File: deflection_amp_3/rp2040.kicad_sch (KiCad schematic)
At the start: 44 parts, among them SW1 RESET, SW2 PROG, U5 W25Q128JVS, U6 RP2040, U7 MCP4822, U8 MCP4822, Y1 ABM8-272-T3

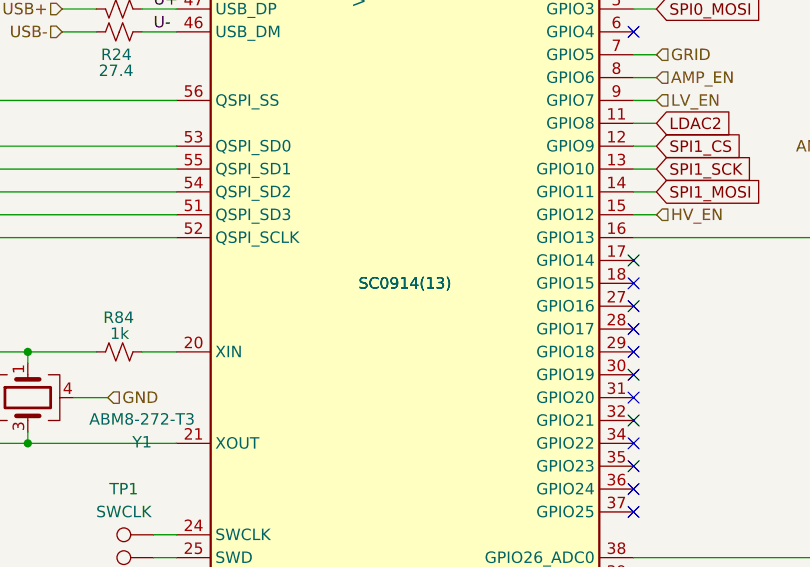
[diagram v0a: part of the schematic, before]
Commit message: fixed BOM + DAC footprint
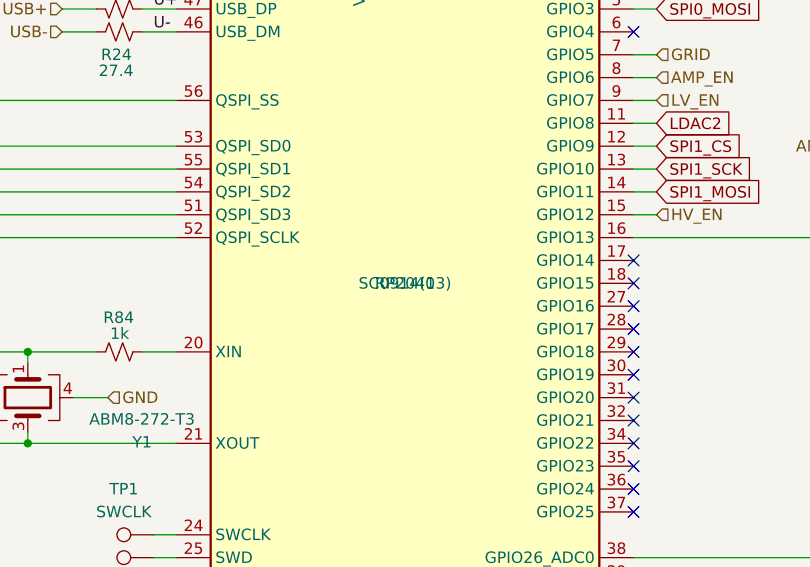
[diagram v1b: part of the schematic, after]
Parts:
- U6: JLCPCB P/N SC0914(13) -> RP2040
- U7, U8: footprint Package_SO:SOIC-8_5.3x5.3mm_P1.27mm -> MCP4822-E_SN:SOIC127P599X175-8N; JLCPCB P/N double check footprint -> MCP4822-E/SN
- Y1: JLCPCB P/N (none) -> ABM8-272-T3
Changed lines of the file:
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@@
 			)
 		)
-		(property "JLCPCB P/N" ""
+		(property "JLCPCB P/N" "ABM8-272-T3"
 			(at 96.52 114.3 0)
 			(effects
@@
 			)
 		)
-		(property "JLCPCB P/N" "SC0914(13)"
+		(property "JLCPCB P/N" "RP2040"
 			(at 138.43 101.6 0)
 			(effects
@@
 			)
 		)
-		(property "Footprint" "Package_SO:SOIC-8_5.3x5.3mm_P1.27mm"
+		(property "Footprint" "MCP4822-E_SN:SOIC127P599X175-8N"
 			(at 262.89 96.52 0)
 			(effects
@@
 			)
 		)
-		(property "JLCPCB P/N" "double check footprint"
+		(property "JLCPCB P/N" "MCP4822-E/SN"
 			(at 242.57 88.9 0)
 			(effects
@@
 			)
 		)
-		(property "Footprint" "Package_SO:SOIC-8_5.3x5.3mm_P1.27mm"
+		(property "Footprint" "MCP4822-E_SN:SOIC127P599X175-8N"
 			(at 262.89 55.88 0)
 			(effects
@@
 			)
 		)
-		(property "JLCPCB P/N" "double check footprint"
+		(property "JLCPCB P/N" "MCP4822-E/SN"
 			(at 242.57 48.26 0)
 			(effects
